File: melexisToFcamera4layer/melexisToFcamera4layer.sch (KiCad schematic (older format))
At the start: 4 parts

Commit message: Voltage sources added
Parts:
- added C? (x14): C, symbol Device:C
- added J? (x5): Conn_01x01, symbol Connector_Generic:Conn_01x01
- added L? (x3): L, symbol Device:L
- added R? (x5): R, symbol Device:R
- added U? (x3): MIC23050, symbol melexisToFcamera4layer_parts:MIC23050
- added U?: LM27762, Package_SON:WSON-12-1EP_3x2mm_P0.5mm_EP1x2.65_ThermalVias, symbol Regulator_SwitchedCapacitor:LM27762
- MK1, MK2, MK3, MK4: symbol Mechanical:Mounting_Hole_PAD -> melexisToFcamera4layer-rescue:Mounting_Hole_PAD-Mechanical
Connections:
- net labels added: +5V, 3V3_clean, ARRAYBIAS, GND, VDD3V3
- wire segments 0 -> 159
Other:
- note added: "1V8 clean"
- note added: "1V8 regular"
- note added: "3V3 regular"
- note added: "Generate negative and 3V3 clean voltages"

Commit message: Added schematics for all power rails
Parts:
- removed U? (x3): MIC23050, symbol melexisToFcamera4layer_parts:MIC23050
- added C? (x3): C, symbol Device:C
- added C?: CP, symbol Device:CP
- added J?: Conn_01x01, symbol Connector_Generic:Conn_01x01
- added L?: L, symbol Device:L
- added R? (x6): R, symbol Device:R
- added U? (x2): MIC23050_GYML, symbol melexisToFcamera4layer_parts:MIC23050_GYML
- added U?: MIC23050_SYML, symbol melexisToFcamera4layer_parts:MIC23050_SYML
- added U?: ADP2164, symbol melexisToFcamera4layer_parts:ADP2164
- MK: renamed from MK1; value Mounting_Hole -> Mounting_Hole_PAD-Mechanical
- MK: renamed from MK3; value Mounting_Hole -> Mounting_Hole_PAD-Mechanical
- MK: renamed from MK2; value Mounting_Hole -> Mounting_Hole_PAD-Mechanical
- MK: renamed from MK4; value Mounting_Hole -> Mounting_Hole_PAD-Mechanical
- gave numbers to parts that had none: 5
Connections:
- net labels added: 1V5
- wire segments 159 -> 240

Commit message: Imported Melexis parts. Next step - verify their connections
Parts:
- added C? (x21): 100n, Capacitors_SMD:C_0603_HandSoldering, symbol Device:C
- added C? (x2): 100u, Capacitors_SMD:C_1206_HandSoldering, symbol Device:C
- added C? (x6): 4u7, Capacitors_SMD:C_0603_HandSoldering, symbol Device:CP
- added C? (x7): 10u, Capacitors_SMD:C_0603_HandSoldering, symbol Device:C
- added C?: 4u7, Capacitors_SMD:C_0603_HandSoldering, symbol Device:C
- added D?: D, symbol Device:D
- added J? (x2): Conn_01x02, symbol Connector_Generic:Conn_01x02
- added L? (x2): L, Resistors_SMD:R_1206_HandSoldering, symbol Device:L
- added R? (x7): 10k, Resistors_SMD:R_0603_HandSoldering, symbol Device:R
- added R?: 500, Resistors_SMD:R_0603_HandSoldering, symbol Device:R
- added U?: MLX75023, symbol melexisToFcamera4layer_parts:MLX75023
- added U?: MLX75123, symbol melexisToFcamera4layer_parts:MLX75123
- added U?: Cmod_A7, symbol melexisToFcamera4layer_parts:Cmod_A7
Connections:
- net +5V: now also J?.2 (Pin_2)
- net 3V3_clean: now also C?.1, U?.21 (PIXELVDD3V3)
- net ARRAYBIAS: now also C?.1, R?.1
- net GND: now also C?.1, C?.1, C?.2, C?.2, C?.2, C?.2, C?.2, C?.2, C?.2, C?.2, C?.2, C?.2, C?.2, C?.2, C?.2, C?.2, C?.2, C?.2, C?.2, C?.2, C?.2, C?.2, C?.2, C?.2, C?.2, C?.2, C?.2, C?.2, C?.2, C?.2, C?.2, C?.2, C?.2, C?.2, C?.2, C?.2, C?.2, R?.1, R?.1, R?.1, R?.2, U?.10 (GND), U?.15 (GND), U?.25 (GND), U?.32 (GND), U?.36 (GND), U?.39 (GND), U?.40 (GND), U?.43 (GND), U?.A11 (GND_IO), U?.A16 (GNDA_1V8), U?.A17 (GND_IO), U?.A18 (GND_IO), U?.A21 (GND_IO), U?.A22 (GNDD_1V8), U?.A24 (GND_IO), U?.A33 (GND_IO), U?.A41 (GND_IO), U?.A5 (GNDA_ADC_1V8), U?.A8 (GND_IO), U?.B10 (GND_IO), U?.B15 (GND_IO), U?.B16 (GND_IO), U?.B18 (GND_IO), U?.B19 (GND_IO), U?.B33 (GND_IO), U?.B8 (GNDA_ADC_1V8), U?.B9 (GNDA_ADC_S_1V8)
- net VDD3V3: now also L?.1, L?.1, R?.1, R?.1
- net 1V5 renamed MIXH_VOLTAGE
- net MIXH_VOLTAGE: now also C?.1, C?.1, C?.1, C?.1, C?.1, C?.1, U?.37 (MIXH_VOLTAGE), U?.38 (MIXH_VOLTAGE), U?.41 (MIXH_VOLTAGE), U?.42 (MIXH_VOLTAGE)
- new net: C?.1, U?.13 (PIXELBIAS)
- new net: R?.2, U?.17 (ARRAYBIAS)
- new net: J?.1 (Pin_1), U?.24 (VU)
- new net A0: U?.14 (OUT0), U?.B6 (A_IN_0)
- new net A1: U?.16 (OUT1), U?.A6 (A_IN_1)
- new net A2: U?.12 (OUT2), U?.A7 (A_IN_2)
- new net A3: U?.11 (OUT3), U?.B7 (A_IN_3)
- new net AVDD3V3: C?.1, C?.1, C?.1, C?.1, C?.1, C?.1, C?.1, L?.2, U?.18 (AVDD3V3), U?.22 (AVDD3V3), U?.B4 (VDDA_3V3)
- new net CLK_IN: U?.17 (PIO17), U?.B13 (CLK_IN)
- new net COL0: U?.30 (COL_0), U?.B37 (COL_0)
- new net COL1: U?.29 (COL_1), U?.A40 (COL_1)
- new net COL2: U?.28 (COL_2), U?.B36 (COL_2)
- new net COL3: U?.27 (COL_3), U?.A39 (COL_3)
- new net COL4: U?.26 (COL_4), U?.B35 (COL_4)
- new net COL5: U?.25 (COL_5), U?.A38 (COL_5)
- new net COL6: U?.24 (COL_6), U?.B34 (COL_6)
- new net COL7: U?.23 (COL_7), U?.A37 (COL_7)
- new net DATA0: U?.5 (PIO05), U?.A30 (DATA_0)
- new net DATA1: U?.6 (PIO06), U?.B27 (DATA_1)
- new net DATA10: U?.15 (AIN15), U?.A25 (DATA_10)
- new net DATA11: U?.16 (AIN16), U?.B22 (DATA_11)
- new net DATA2: U?.7 (PIO07), U?.A29 (DATA_2)
- new net DATA3: U?.8 (PIO08), U?.B26 (DATA_3)
- new net DATA4: U?.9 (PIO09), U?.A28 (DATA_4)
- new net DATA5: U?.10 (PIO10), U?.B25 (DATA_5)
- new net DATA6: U?.11 (PIO11), U?.A27 (DATA_6)
- new net DATA7: U?.12 (PIO12), U?.B24 (DATA_7)
- new net DATA8: U?.13 (PIO13), U?.A26 (DATA_8)
- new net DATA9: U?.14 (PIO14), U?.B23 (DATA_9)
- new net DMIX+: R?.2, U?.35 (DMIX_0), U?.A35 (DMIX_0)
- new net DMIX-: R?.2, U?.34 (DMIX_1), U?.B32 (DMIX_1)
- new net DVDD3V3: C?.1, C?.1, C?.1, C?.1, C?.1, C?.1, C?.1, C?.1, C?.1, C?.1, C?.2, C?.2, D?.1 (K), L?.2, R?.1, U?.33 (DVDD3V3), U?.44 (DVDD3V3), U?.A36 (VDDD_3V3), U?.B12 (VDD_I2C), U?.B17 (VDDD_3V3), U?.B21 (VDD_IO), U?.B30 (VDD_IO), U?.B38 (VDDD_3V3)
- new net FLUSH: U?.19 (PIXELFLUSH), U?.B3 (FLUSH)
- new net FSYNC: U?.3 (PIO03), U?.A31 (FSYNC)
- new net HSYNC: U?.2 (PIO02), U?.B29 (HSYNC)
- new net LATCHEN: R?.2, U?.9 (LATCH_ENABLE), U?.A4 (LATCH_EN)
- new net LEDN: J?.1 (Pin_1), R?.2, U?.A34 (LEDN)
- new net LEDP: J?.2 (Pin_2), R?.1, U?.B31 (LEDP)
- new net PIXCLK: U?.4 (PIO04), U?.B28 (PIXCLK)
- new net QUIET: U?.18 (PIO18), U?.A15 (QUIET)
- new net RESET: U?.19 (PIO19), U?.A14 (RESET_IN)
- new net RESETOUT: U?.20 (CORE_RESET), U?.A3 (ARRAY_RST)
- new net ROW0: U?.8 (ROW_0), U?.A42 (ROW_0)
- new net ROW1: U?.7 (ROW_1), U?.B39 (ROW_1)
- new net ROW2: U?.6 (ROW_2), U?.A43 (ROW_2)
- new net ROW3: U?.5 (ROW_3), U?.B40 (ROW_3)
- new net ROW4: U?.4 (ROW_4), U?.A44 (ROW_4)
- new net ROW5: U?.3 (ROW_5), U?.A1 (ROW_5)
- new net ROW6: U?.2 (ROW_6), U?.B1 (ROW_6)
- new net ROW7: U?.1 (ROW_7), U?.A2 (ROW_7)
- new net SCL: R?.2, U?.21 (PIO21), U?.A12 (SCL)
- new net SDA: R?.2, U?.22 (PIO22), U?.B11 (SDA)
- new net SHUTTER: U?.31 (SHUTTER), U?.B2 (SHUT)
- new net TRIGGER: U?.20 (PIO20), U?.A13 (TRIGGER_IN)
- new net VDD1V8: C?.1, C?.1, C?.1, D?.2 (A), U?.B20 (VDDD_1V8)
- new net VDD1V8_clean: C?.1, C?.1, C?.1, C?.1, C?.1, C?.1, U?.A10 (VDDA_ADC_S_1V8), U?.A9 (VDDA_ADC_1V8), U?.B14 (VDDA_1V8), U?.B5 (VDDA_ADC_1V8)
- new net VSYNC: U?.1 (PIO01), U?.A32 (VSYNC)
- no-connect marks 4 -> 7
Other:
- note added: "In this scenario we suggest to connect certain domains to each other with good decoupling techniques.\n1V8 : VDDD_1V8, VDD_IO, VDD_I2C\n1V8_Clean : VDDA_1V8, VDDA_ADC_1V8, VDDA_ADC_S_1V8\n3V3 : VDDA_3V3, VDDD_3V3\n\nIn combination with MLX75023 or MLX75024 an extra MIXH regulator, 3V3_clean and negative ARRAYBIAS supply is\nrequired."
- note added: "Optional CEC!"
- moved on the sheet: MK

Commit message: Test commit, changed credentials
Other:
- note removed: "Optional CEC!"
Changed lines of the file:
@@
 	0    -1   -1   0
 $EndComp
-Text Notes 14400 400  0    60   ~ 0
-Optional CEC!
 Text Label 9350 6200 2    60   ~ 0
 LEDN

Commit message: Added component values in the schematic of sensor board
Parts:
- C12: renamed from C?; value C -> 1u
- C17, C2: renamed from C; value C -> 10u
- C23, C24: renamed from C; value C -> 2u2
- C27: renamed from C?; value C -> 100n
- C31: renamed from C?; value C -> 10u
- C35, C37, C38, C43, C44, C55: renamed from C; value C -> 4u7
- C36, C42, C53: renamed from C; value C -> 560p
- C6: renamed from C?; value CP -> 150u
- C8: renamed from C; value C -> 1u
- L4, L5, L6: renamed from L; value L -> 1u
- R1: renamed from R; value R -> 10k
- R10: renamed from R; value R -> 316k
- R11: renamed from R; value R -> 511k
- R12: renamed from R; value R -> 549k
- R13, R4: renamed from R?; value R -> 10k
- R14: renamed from R?; value R -> 10R
- R6: renamed from R?; value R -> 27k
- R7: renamed from R?; value R -> X
- R8: renamed from R?; value R -> Y
- R9: renamed from R; value R -> 953k
- gave numbers to parts that had none: 59
- renumbered J to J2, J to J3, J to J5, J to J7, J to J8, MK to MK1, MK to MK2, MK to MK3, MK to MK4, U to U1
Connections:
- no-connect marks 7 -> 28

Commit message: Assigned footprints to the components on sensor board's schematic
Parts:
- C1, C10, C11, C13, C14, C15, C16, C18, C19, C20, C21, C22, C25, C28, C29, C3, C30, C32, C33, C39, C4, C40, C41, C45, C46, C47, C48, C49, C5, C50, C51, C52, C54, C7, C9: footprint Capacitors_SMD:C_0603_HandSoldering -> Capacitors_SMD:C_0603
- C12, C17, C2, C23, C24, C27, C31, C35, C36, C37, C38, C42, C43, C44, C53, C55, C6, C8: footprint (none) -> Capacitors_SMD:C_0603
- C26, C34: footprint Capacitors_SMD:C_1206_HandSoldering -> Capacitors_SMD:C_0603
- D1: footprint (none) -> Diodes_SMD:D_0805
- J1, J2, J3, J5, J7, J8: footprint (none) -> Measurement_Points:Measurement_Point_Round-SMD-Pad_Small
- J4, J6: footprint (none) -> Socket_Strips:Socket_Strip_Angled_1x02_Pitch2.54mm
- L3, L4, L5, L6: footprint (none) -> Resistors_SMD:R_1206_HandSoldering
- R1, R13, R4: footprint (none) -> Resistors_SMD:R_0603
- R10, R11, R12, R14, R6, R7, R8, R9: footprint (none) -> Resistors_SMD:R_0805_HandSoldering
- R15, R16, R17, R18, R19, R2, R3: footprint Resistors_SMD:R_0603_HandSoldering -> Resistors_SMD:R_0603
- R5: footprint Resistors_SMD:R_0603_HandSoldering -> Resistors_SMD:R_0805_HandSoldering

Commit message: Added and assigned footprints to sensor board. One still missing :-(
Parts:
- U3: footprint (none) -> footprintsForCamera:MLX75023
- U4, U6, U7: footprint (none) -> footprintsForCamera:MIC23050
- U5: footprint (none) -> footprintsForCamera:Cmod_A7
- U8: footprint (none) -> footprintsForCamera:MLX75123
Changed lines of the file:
@@
 F 0 "U6" H 10550 2165 50  0000 C CNN
 F 1 "MIC23050_GYML" H 10550 2074 50  0000 C CNN
-F 2 "" H 10450 1850 50  0001 C CNN
+F 2 "footprintsForCamera:MIC23050" H 10450 1850 50  0001 C CNN
 F 3 "" H 10450 1850 50  0001 C CNN
 	1    10450 1700
@@
 F 0 "U4" H 7050 2165 50  0000 C CNN
 F 1 "MIC23050_SYML" H 7050 2074 50  0000 C CNN
-F 2 "" H 6950 1850 50  0001 C CNN
+F 2 "footprintsForCamera:MIC23050" H 6950 1850 50  0001 C CNN
 F 3 "" H 6950 1850 50  0001 C CNN
 	1    6950 1700
@@
 F 0 "U7" H 14100 2165 50  0000 C CNN
 F 1 "MIC23050_GYML" H 14100 2074 50  0000 C CNN
-F 2 "" H 14000 1850 50  0001 C CNN
+F 2 "footprintsForCamera:MIC23050" H 14000 1850 50  0001 C CNN
 F 3 "" H 14000 1850 50  0001 C CNN
 	1    14000 1700
@@
 F 0 "U3" H 2650 9750 60  0000 C CNN
 F 1 "MLX75023" H 3600 7250 60  0000 C CNN
-F 2 "" H 3350 8400 60  0001 C CNN
+F 2 "footprintsForCamera:MLX75023" H 3350 8400 60  0001 C CNN
 F 3 "" H 3350 8400 60  0000 C CNN
 	1    3350 8350
@@
 F 0 "U8" H 11250 6600 60  0000 C CNN
 F 1 "MLX75123" H 12400 1900 60  0000 C CNN
-F 2 "" H 11700 5250 60  0001 C CNN
+F 2 "footprintsForCamera:MLX75123" H 11700 5250 60  0001 C CNN
 F 3 "" H 11700 5250 60  0000 C CNN
 	1    15300 5100
@@
 F 0 "U5" H 7600 4850 60  0000 C CNN
 F 1 "Cmod_A7" H 7600 4750 60  0000 C CNN
-F 2 "" H 7600 4850 60  0001 C CNN
+F 2 "footprintsForCamera:Cmod_A7" H 7600 4850 60  0001 C CNN
 F 3 "" H 7600 4850 60  0000 C CNN
 	1    7600 4800

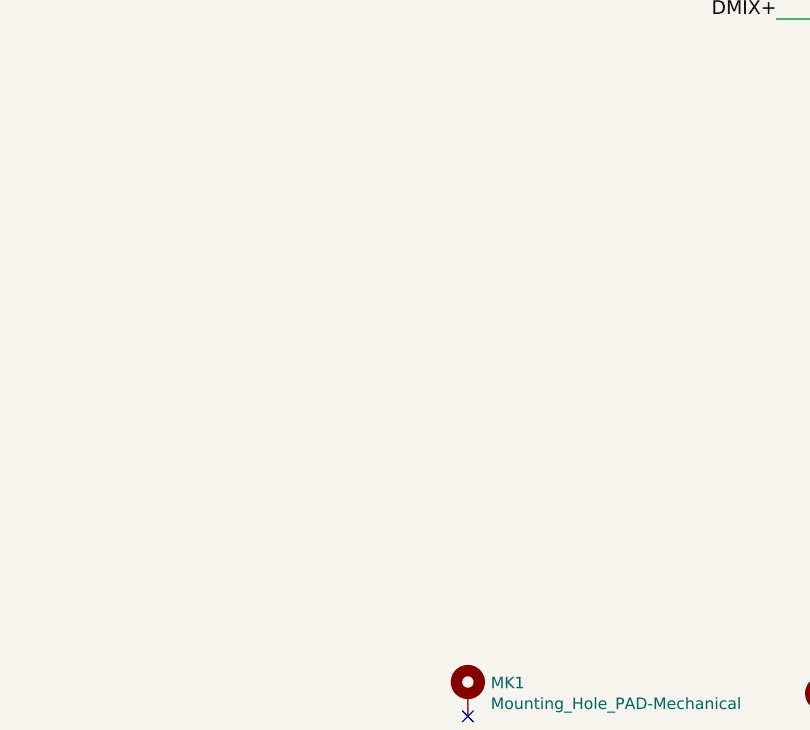
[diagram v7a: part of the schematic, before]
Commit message: Finalized adding footprints for sensor board, starting routing it.
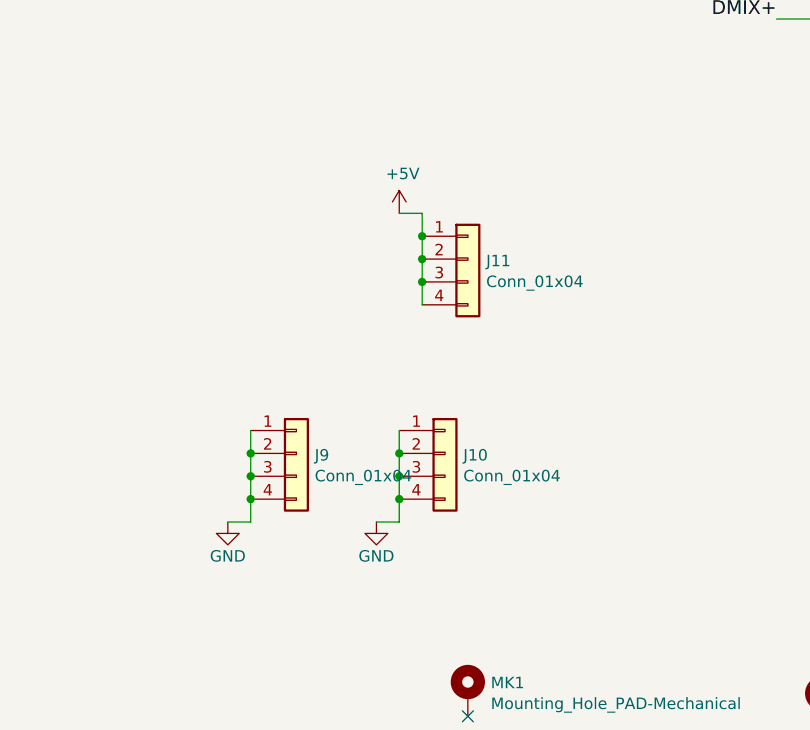
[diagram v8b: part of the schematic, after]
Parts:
- added J10, J11, J9: Conn_01x04, Pin_Headers:Pin_Header_Straight_1x04_Pitch2.54mm, symbol Connector_Generic:Conn_01x04
- J4, J6: footprint Socket_Strips:Socket_Strip_Angled_1x02_Pitch2.54mm -> Pin_Headers:Pin_Header_Straight_1x02_Pitch2.54mm
- U1: footprint Package_SON:WSON-12-1EP_3x2mm_P0.5mm_EP1x2.65_ThermalVias -> footprintsForCamera:LM27762
- U2: footprint (none) -> footprintsForCamera:ADP2164
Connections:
- net +5V: now also J11.1 (Pin_1), J11.2 (Pin_2), J11.3 (Pin_3), J11.4 (Pin_4)
- net GND: now also J10.1 (Pin_1), J10.2 (Pin_2), J10.3 (Pin_3), J10.4 (Pin_4), J9.1 (Pin_1), J9.2 (Pin_2), J9.3 (Pin_3), J9.4 (Pin_4)
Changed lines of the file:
@@
 F 0 "U1" H 2300 1967 50  0000 C CNN
 F 1 "LM27762" H 2300 1876 50  0000 C CNN
-F 2 "Package_SON:WSON-12-1EP_3x2mm_P0.5mm_EP1x2.65_ThermalVias" H 2400 750 50  0001 L CNN
+F 2 "footprintsForCamera:LM27762" H 2400 750 50  0001 L CNN
 F 3 "http://www.ti.com/lit/ds/symlink/lm27762.pdf" H 4750 1100 50  0001 C CNN
 	1    2250 1500
@@
 F 0 "U2" H 3350 4465 50  0000 C CNN
 F 1 "ADP2164" H 3350 4374 50  0000 C CNN
-F 2 "" H 3350 3850 50  0001 C CNN
+F 2 "footprintsForCamera:ADP2164" H 3350 3850 50  0001 C CNN
 F 3 "" H 3350 3850 50  0001 C CNN
 	1    3350 3850
@@
 F 0 "J4" V 6472 6180 50  0000 L CNN
 F 1 "Conn_01x02" V 6563 6180 50  0000 L CNN
-F 2 "Socket_Strips:Socket_Strip_Angled_1x02_Pitch2.54mm" H 6600 6100 50  0001 C CNN
+F 2 "Pin_Headers:Pin_Header_Straight_1x02_Pitch2.54mm" H 6600 6100 50  0001 C CNN
 F 3 "~" H 6600 6100 50  0001 C CNN
 	1    6600 6100
@@
 F 0 "J6" H 10080 6192 50  0000 L CNN
 F 1 "Conn_01x02" H 10080 6101 50  0000 L CNN
-F 2 "Socket_Strips:Socket_Strip_Angled_1x02_Pitch2.54mm" H 10000 6200 50  0001 C CNN
+F 2 "Pin_Headers:Pin_Header_Straight_1x02_Pitch2.54mm" H 10000 6200 50  0001 C CNN
 F 3 "~" H 10000 6200 50  0001 C CNN
 	1    10000 6200
@@
 NoConn ~ 8400 5700
 NoConn ~ 8400 5800
+$Comp
+L Connector_Generic:Conn_01x04 J11
+U 1 1 5CB4F921
+P 8200 8450
+F 0 "J11" H 8280 8442 50  0000 L CNN
+F 1 "Conn_01x04" H 8280 8351 50  0000 L CNN
+F 2 "Pin_Headers:Pin_Header_Straight_1x04_Pitch2.54mm" H 8200 8450 50  0001 C CNN
+F 3 "~" H 8200 8450 50  0001 C CNN
+	1    8200 8450
+	1    0    0    -1
+$EndComp
+$Comp
+L Connector_Generic:Conn_01x04 J9
+U 1 1 5CB500EB
+P 7450 9300
+F 0 "J9" H 7530 9292 50  0000 L CNN
+F 1 "Conn_01x04" H 7530 9201 50  0000 L CNN
+F 2 "Pin_Headers:Pin_Header_Straight_1x04_Pitch2.54mm" H 7450 9300 50  0001 C CNN
+F 3 "~" H 7450 9300 50  0001 C CNN
+	1    7450 9300
+	1    0    0    -1
+$EndComp
+$Comp
+L Connector_Generic:Conn_01x04 J10
+U 1 1 5CB5087B
+P 8100 9300
+F 0 "J10" H 8180 9292 50  0000 L CNN
+F 1 "Conn_01x04" H 8180 9201 50  0000 L CNN
+F 2 "Pin_Headers:Pin_Header_Straight_1x04_Pitch2.54mm" H 8100 9300 50  0001 C CNN
+F 3 "~" H 8100 9300 50  0001 C CNN
+	1    8100 9300
+	1    0    0    -1
+$EndComp
+$Comp
+L power:GND #PWR034
+U 1 1 5CB511C8
+P 7800 9600
+F 0 "#PWR034" H 7800 9350 50  0001 C CNN
+F 1 "GND" H 7800 9450 50  0000 C CNN
+F 2 "" H 7800 9600 50  0001 C CNN
+F 3 "" H 7800 9600 50  0001 C CNN
+	1    7800 9600
+	1    0    0    -1
+$EndComp
+$Comp
+L power:GND #PWR033
+U 1 1 5CB51EA2
+P 7150 9600
+F 0 "#PWR033" H 7150 9350 50  0001 C CNN
+F 1 "GND" H 7150 9450 50  0000 C CNN
+F 2 "" H 7150 9600 50  0001 C CNN
+F 3 "" H 7150 9600 50  0001 C CNN
+	1    7150 9600
+	1    0    0    -1
+$EndComp
+Wire Wire Line
+	7250 9200 7250 9300
+Wire Wire Line
+	7250 9600 7150 9600
+Connection ~ 7250 9300
+Wire Wire Line
+	7250 9300 7250 9400
+Connection ~ 7250 9400
+Wire Wire Line
+	7250 9400 7250 9500
+Connection ~ 7250 9500
+Wire Wire Line
+	7250 9500 7250 9600
+Wire Wire Line
+	7900 9200 7900 9300
+Wire Wire Line
+	7900 9600 7800 9600
+Connection ~ 7900 9300
+Wire Wire Line
+	7900 9300 7900 9400
+Connection ~ 7900 9400
+Wire Wire Line
+	7900 9400 7900 9500
+Connection ~ 7900 9500
+Wire Wire Line
+	7900 9500 7900 9600
+$Comp
+L power:+5V #PWR035
+U 1 1 5CC2799B
+P 7900 8250
+F 0 "#PWR035" H 7900 8100 50  0001 C CNN
+F 1 "+5V" H 7915 8423 50  0000 C CNN
+F 2 "" H 7900 8250 50  0001 C CNN
+F 3 "" H 7900 8250 50  0001 C CNN
+	1    7900 8250
+	1    0    0    -1
+$EndComp
+Wire Wire Line
+	8000 8650 8000 8550
+Wire Wire Line
+	8000 8250 7900 8250
+Connection ~ 8000 8350
+Wire Wire Line
+	8000 8350 8000 8250
+Connection ~ 8000 8450
+Wire Wire Line
+	8000 8450 8000 8350
+Connection ~ 8000 8550
+Wire Wire Line
+	8000 8550 8000 8450
 $EndSCHEMATC
